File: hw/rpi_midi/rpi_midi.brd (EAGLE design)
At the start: 38.4 x 37.5 mm, 51 parts, among them IC1 74HC14D, IC2 TL331, IC3 6N138, IC4 6N138, X1 WBTOR12.54MM, X2 WBTOR12.54MM, X3 WBTOR12.54MM, X4 WBTOR12.54MM

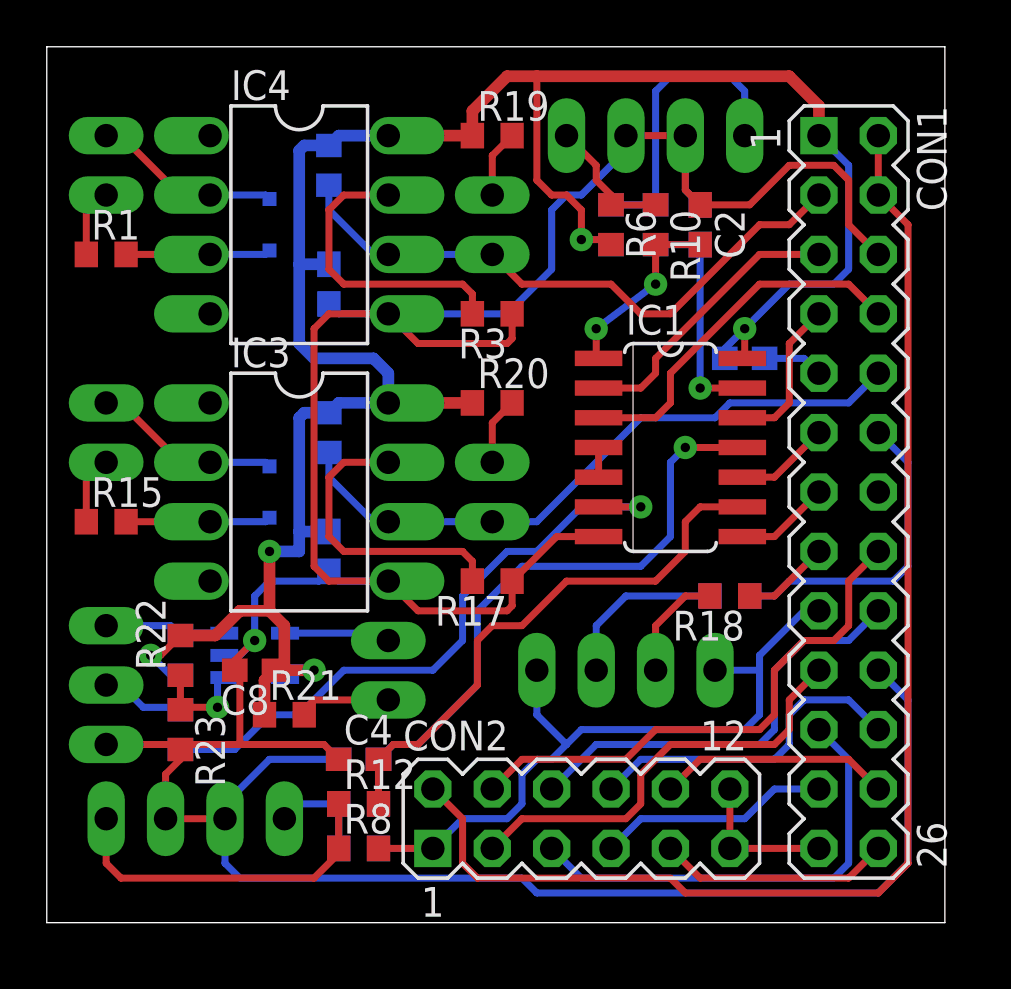
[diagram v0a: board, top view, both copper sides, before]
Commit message: Updated the RPi MIDI hardware layout file with a silkscreen layer
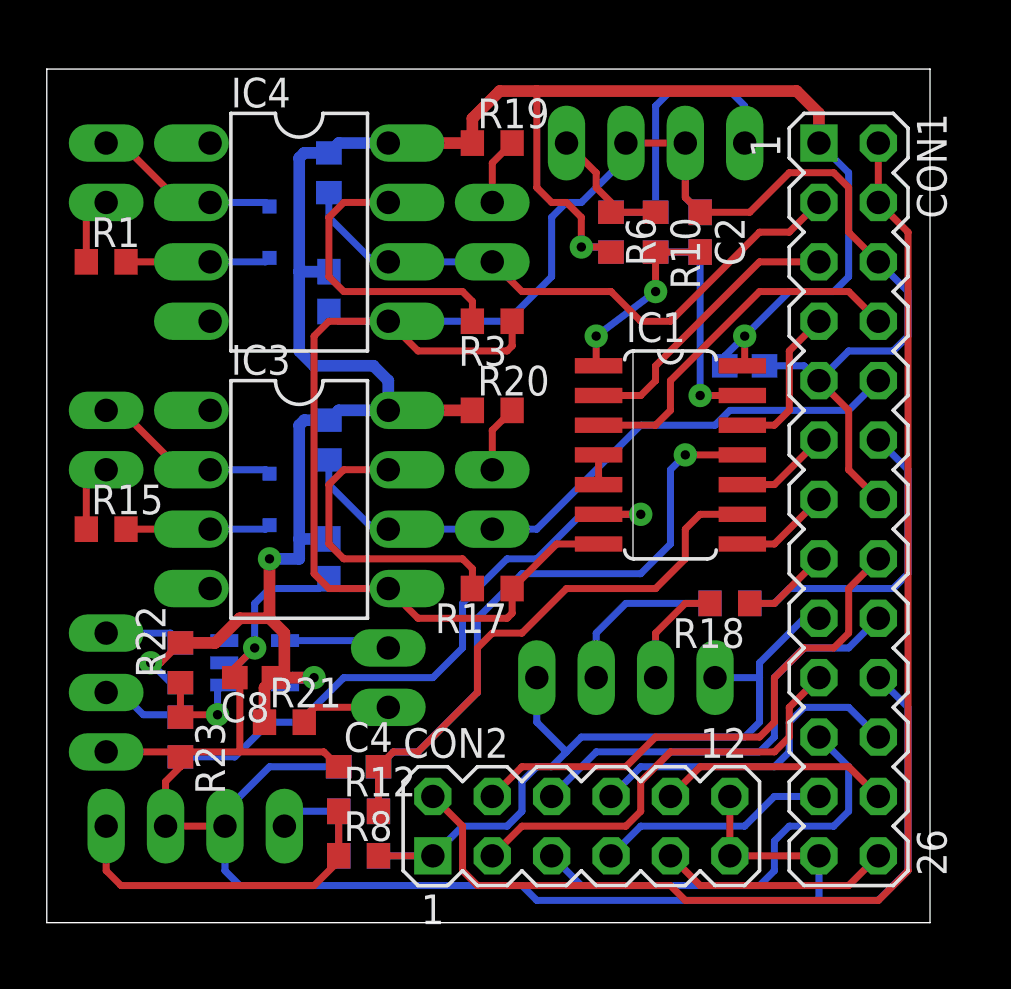
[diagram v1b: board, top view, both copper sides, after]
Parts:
- moved R19 0.32 mm to (19.1, 33.3)
- moved R20 0.32 mm to (19.1, 21.9)
- moved X1 0.32 mm to (23.5, 33.3)
- moved X2 0.32 mm to (28.6, 33.3)
- moved C7 0.32 mm to (12.1, 15.6)
- moved C8 0.32 mm to (8.89, 10.5)
- moved LED1 0.32 mm to (22.2, 10.5)
- moved LED2 0.32 mm to (27.3, 10.5)
- moved LED5 0.32 mm to (14.6, 10.5)
- moved MIDI_OUT 0.32 mm to (2.54, 9.84)
- moved R14 0.32 mm to (29.2, 13.7)
- moved R17 0.32 mm to (19.1, 14.3)
- moved R18 0.32 mm to (29.2, 13.7)
- moved R21 0.32 mm to (10.2, 8.57)
- moved R23 0.32 mm to (5.71, 7.94)
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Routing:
- net GND: track 160.4 -> 176.7 mm
- net GPIO9_MISO: track 19.7 -> 19.0 mm
- net N$14: track 13.0 -> 12.4 mm
- net +3V3: track 133.7 -> 133.1 mm
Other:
- board size 38.4 x 37.5 mm -> 37.8 x 36.5 mm
- board text added: "1"
- board text added: "FS/RS/DS"
- board text added: "IN1"
- board text added: "IN2"
- board text added: "J1"
- board text added: "J2"
- board text added: "J3"
- board text added: "J4"
- board text added: "L1"
- board text added: "L2"
- board text added: "MiDiPi"
- board text added: "OUT"
- board text added: "v1.0"

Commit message: Updated the MIDI extension hardware layout file. Optimized the routing of several signals to avoid sharp-angled fanouts
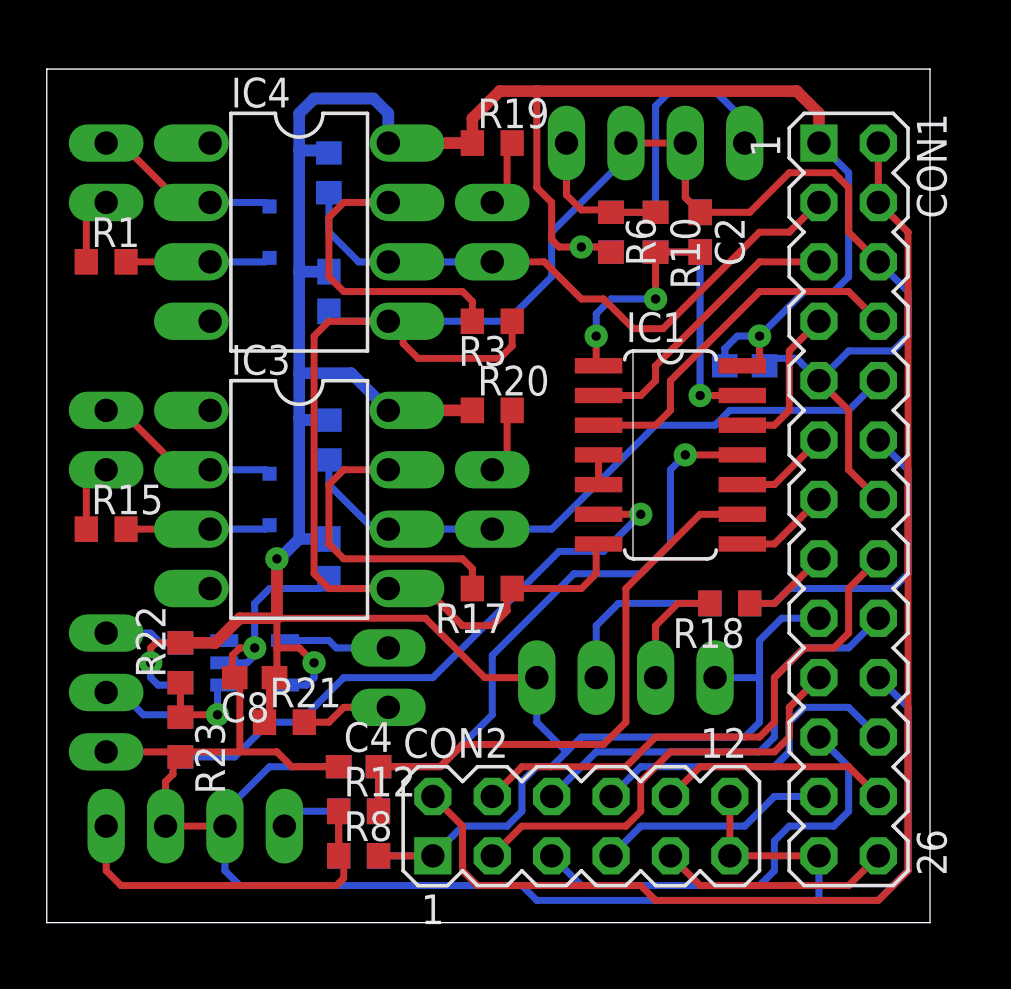
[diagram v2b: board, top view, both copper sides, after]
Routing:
- net +3V3: track 133.1 -> 154.4 mm
- net GND: track 176.7 -> 179.0 mm
- net N$18: track 23.8 -> 25.3 mm
- net N$6: track 26.9 -> 25.8 mm
- net N$13: track 8.14 -> 9.04 mm
- net N$15: track 14.7 -> 15.4 mm
- net N$12: track 5.65 -> 6.34 mm
- net GPIO2_SDA: track 26.0 -> 26.6 mm
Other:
- board text added: "S1"
- board text added: "S2"
- board text added: "S3"
- board text added: "S4"
- board text removed: "J1"
- board text removed: "J2"
- board text removed: "J3"
- board text removed: "J4"
